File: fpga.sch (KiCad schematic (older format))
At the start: 4 parts

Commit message: FPGA change and new project file
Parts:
- removed U? (x4): XC6SLX9-2TQG144I, symbol FPGA_Xilinx_Spartan6:XC6SLX4-TQG144
- added U?: XC7S6-1FTGB196C, Xilinx-XC7S6-1FTGB196C-0-0-*, symbol sdr:XC7S6-1FTGB196C
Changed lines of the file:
@@
 $Descr A4 11693 8268
 encoding utf-8
-Sheet 1 1
+Sheet 1 12
 Title "Open HF SDR FPGA Sheet"
 Date "2021-01-16"
@@
 $EndDescr
 $Comp
-L FPGA_Xilinx_Spartan6:XC6SLX4-TQG144 U?
-U 1 1 6003554A
-P 3100 2500
-F 0 "U?" H 3100 725 50  0000 C CNN
-F 1 "XC6SLX9-2TQG144I" H 3100 634 50  0000 C CNN
-F 2 "" H 3100 2500 50  0001 C CNN
-F 3 "http://www.farnell.com/datasheets/1763510.pdf" H 3100 543 50  0000 C CNN
-F 4 "2831296 " H 3100 2500 50  0001 C CNN "Farnell"
-	1    3100 2500
+L sdr:XC7S6-1FTGB196C U?
+U 2 1 6006B8ED
+P 4150 1600
+F 0 "U?" H 6100 1865 50  0000 C CNN
+F 1 "XC7S6-1FTGB196C" H 6100 1774 50  0000 C CNN
+F 2 "Xilinx-XC7S6-1FTGB196C-0-0-*" H 4150 2000 50  0001 L CNN
+F 3 "https://www.xilinx.com/support/documentation/data_sheets/ds189-spartan-7-data-sheet.pdf" H 4150 2100 50  0001 L CNN
+F 4 "180Kbits" H 4150 2200 50  0001 L CNN "RAM size"
+F 5 "No" H 4150 2300 50  0001 L CNN "automotive"
+F 6 "IC" H 4150 2400 50  0001 L CNN "category"
+F 7 "Integrated Circuits (ICs)" H 4150 2500 50  0001 L CNN "device class L1"
+F 8 "Embedded Processors and Controllers" H 4150 2600 50  0001 L CNN "device class L2"
+F 9 "FPGAs - Field Programmable Gate Arrays" H 4150 2700 50  0001 L CNN "device class L3"
+F 10 "XC7S6-1FTGB196C" H 4150 2800 50  0001 L CNN "digikey description"
+F 11 "122-2240-ND" H 4150 2900 50  0001 L CNN "digikey part number"
+F 12 "https://www.xilinx.com/support/documentation/user_guides/ug475_7Series_Pkg_Pinout.pdf" H 4150 3000 50  0001 L CNN "footprint url"
+F 13 "200MHz" H 4150 3100 50  0001 L CNN "frequency"
+F 14 "1.55mm" H 4150 3200 50  0001 L CNN "height"
+F 15 "BGA196C100P14X14_1500X1500X146" H 4150 3300 50  0001 L CNN "ipc land pattern name"
+F 16 "Yes" H 4150 3400 50  0001 L CNN "lead free"
+F 17 "d5f555df3775b1ed" H 4150 3500 50  0001 L CNN "library id"
+F 18 "Xilinx" H 4150 3600 50  0001 L CNN "manufacturer"
+F 19 "+85°C" H 4150 3700 50  0001 L CNN "max junction temp"
+F 20 "3.465V" H 4150 3800 50  0001 L CNN "max supply voltage"
+F 21 "0.95V" H 4150 3900 50  0001 L CNN "min supply voltage"
+F 22 "100" H 4150 4000 50  0001 L CNN "number of I/Os"
+F 23 "938" H 4150 4100 50  0001 L CNN "number of logic blocks"
+F 24 "6000" H 4150 4200 50  0001 L CNN "number of logic elements cells"
+F 25 "FTGB196" H 4150 4300 50  0001 L CNN "package"
+F 26 "0.13ns" H 4150 4400 50  0001 L CNN "propagation delay"
+F 27 "Yes" H 4150 4500 50  0001 L CNN "rohs"
+F 28 "1" H 4150 4600 50  0001 L CNN "speed grade"
+F 29 "0.3mm" H 4150 4700 50  0001 L CNN "standoff height"
+F 30 "+85°C" H 4150 4800 50  0001 L CNN "temperature range high"
+F 31 "0°C" H 4150 4900 50  0001 L CNN "temperature range low"
+	2    4150 1600
 	1    0    0    -1
 $EndComp
-$Comp
-L FPGA_Xilinx_Spartan6:XC6SLX4-TQG144 U?
-U 2 1 6003A903
-P 8700 2550
-F 0 "U?" H 8700 775 50  0000 C CNN
-F 1 "XC6SLX9-2TQG144I" H 8700 684 50  0000 C CNN
-F 2 "" H 8700 2550 50  0001 C CNN
-F 3 "http://www.farnell.com/datasheets/1763510.pdf" H 8700 2550 50  0000 C CNN
-	2    8700 2550
-	1    0    0    -1
-$EndComp
-$Comp
-L FPGA_Xilinx_Spartan6:XC6SLX4-TQG144 U?
-U 3 1 60040928
-P 2700 5750
-F 0 "U?" H 2832 6517 50  0000 C CNN
-F 1 "XC6SLX9-2TQG144I" H 2832 6426 50  0000 C CNN
-F 2 "" H 2700 5750 50  0001 C CNN
-F 3 "http://www.farnell.com/datasheets/1763510.pdf" H 2700 5750 50  0000 C CNN
-	3    2700 5750
-	1    0    0    -1
-$EndComp
-$Comp
-L FPGA_Xilinx_Spartan6:XC6SLX4-TQG144 U?
-U 4 1 600436B6
-P 8700 5600
-F 0 "U?" H 8700 6467 50  0000 C CNN
-F 1 "XC6SLX9-2TQG144I" H 8700 6376 50  0000 C CNN
-F 2 "" H 8700 5600 50  0001 C CNN
-F 3 "http://www.farnell.com/datasheets/1763510.pdf" H 8700 5600 50  0000 C CNN
-	4    8700 5600
-	1    0    0    -1
-$EndComp

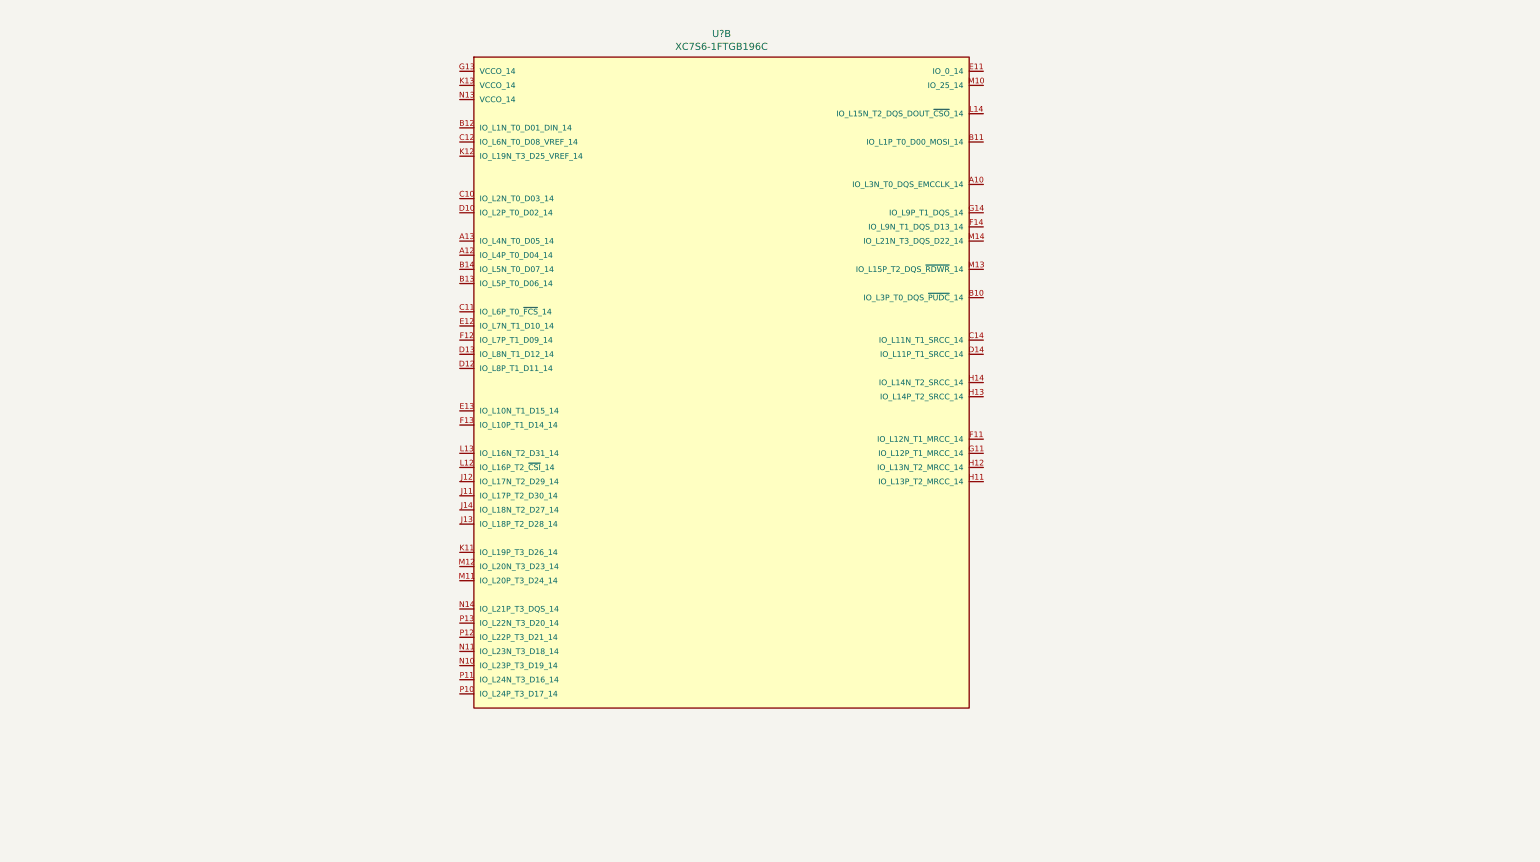
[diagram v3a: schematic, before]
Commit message: SDR-FPGA Interface v0
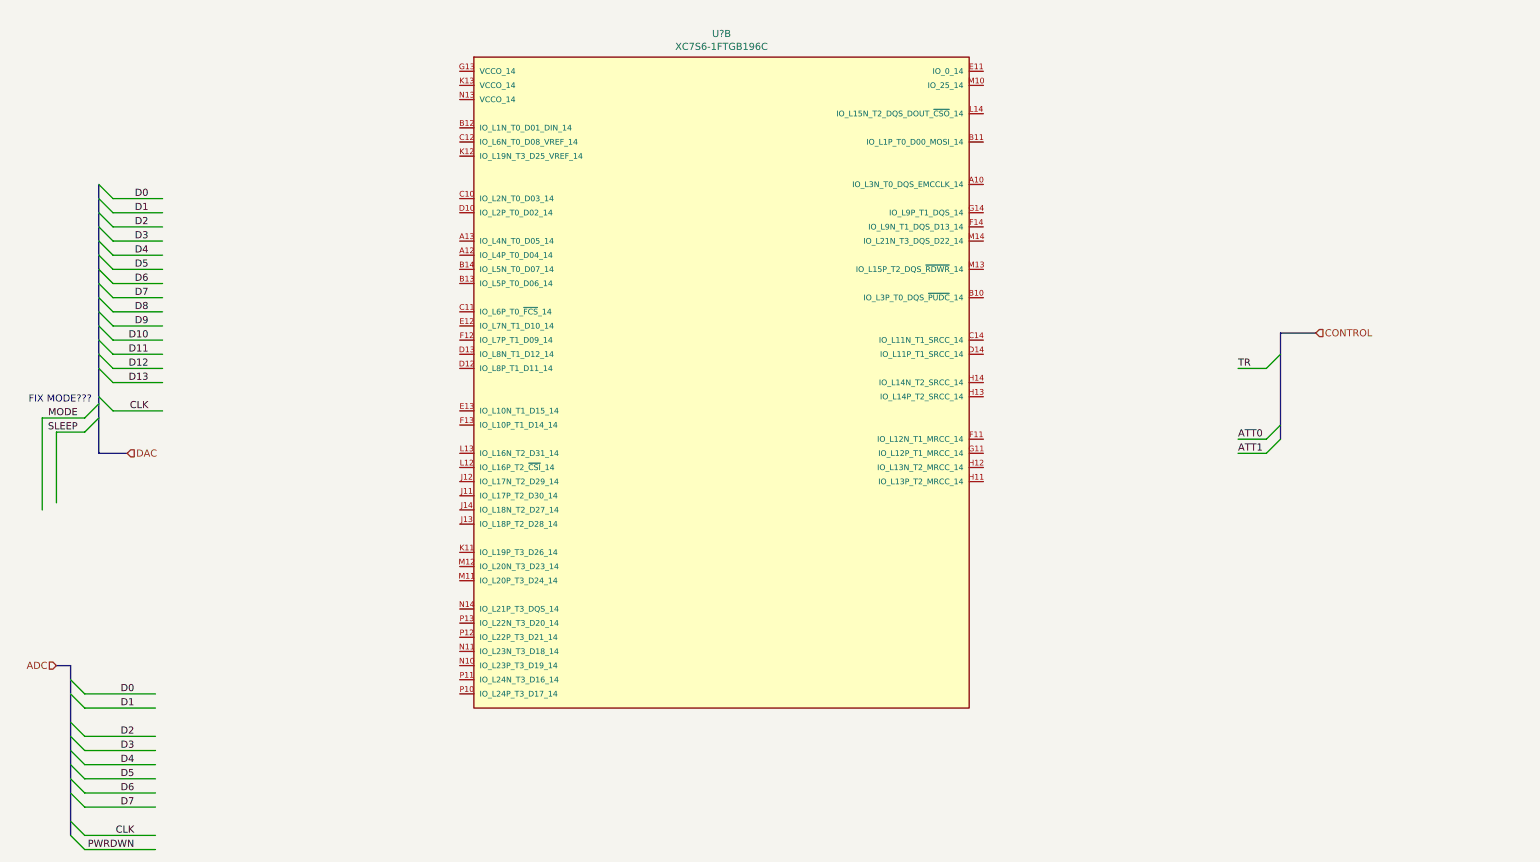
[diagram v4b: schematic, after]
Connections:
- net labels added: ADC, ATT0, ATT1, CLK, CONTROL, D0, D1, D10, D11, D12, D13, D2, D3, D4, D5, D6, D7, D8, D9, DAC, MODE, PWRDWN, SLEEP, TR
- wire segments 0 -> 32
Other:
- note added: "FIX MODE???"
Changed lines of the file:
@@
 	1    0    0    -1
 $EndComp
+Text HLabel 1400 5800 0    50   Input ~ 0
+ADC
+Entry Wire Line
+	1500 5900 1600 6000
+Entry Wire Line
+	1600 6100 1500 6000
+Entry Wire Line
+	1600 6300 1500 6200
+Entry Wire Line
+	1600 6400 1500 6300
+Entry Wire Line
+	1600 6500 1500 6400
+Entry Wire Line
+	1600 6600 1500 6500
+Entry Wire Line
+	1600 6700 1500 6600
+Entry Wire Line
+	1600 6800 1500 6700
+Entry Wire Line
+	1600 7000 1500 6900
+Entry Wire Line
+	1600 7100 1500 7000
+Wire Wire Line
+	2100 6000 1600 6000
+Wire Wire Line
+	2100 6100 1600 6100
+Wire Wire Line
+	1600 6300 2100 6300
+Wire Wire Line
+	2100 6400 1600 6400
+Wire Wire Line
+	2100 6500 1600 6500
+Wire Wire Line
+	2100 6600 1600 6600
+Wire Wire Line
+	2100 6700 1600 6700
+Wire Wire Line
+	2100 6800 1600 6800
+Wire Wire Line
+	2100 7000 1600 7000
+Wire Wire Line
+	2100 7100 1600 7100
+Text Label 1950 6000 2    50   ~ 0
+D0
+Text Label 1950 6100 2    50   ~ 0
+D1
+Text Label 1950 6300 2    50   ~ 0
+D2
+Text Label 1950 6400 2    50   ~ 0
+D3
+Text Label 1950 6500 2    50   ~ 0
+D4
+Text Label 1950 6600 2    50   ~ 0
+D5
+Text Label 1950 6700 2    50   ~ 0
+D6
+Text Label 1950 6800 2    50   ~ 0
+D7
+Text Label 1950 7000 2    50   ~ 0
+CLK
+Text Label 1950 7100 2    50   ~ 0
+PWRDWN
+Wire Bus Line
+	1500 5800 1400 5800
+Entry Wire Line
+	1800 2500 1700 2400
+Entry Wire Line
+	1800 2600 1700 2500
+Entry Wire Line
+	1800 2700 1700 2600
+Entry Wire Line
+	1800 2800 1700 2700
+Entry Wire Line
+	1800 2900 1700 2800
+Entry Wire Line
+	1800 3000 1700 2900
+Entry Wire Line
+	1800 3100 1700 3000
+Entry Wire Line
+	1800 3200 1700 3100
+Entry Wire Line
+	1800 3300 1700 3200
+Entry Wire Line
+	1800 3400 1700 3300
+Entry Wire Line
+	1800 3500 1700 3400
+Entry Wire Line
+	1800 3600 1700 3500
+Entry Wire Line
+	1800 3700 1700 3600
+Entry Wire Line
+	1800 3800 1700 3700
+Entry Wire Line
+	1800 4000 1700 3900
+Wire Wire Line
+	2150 2500 1800 2500
+Wire Wire Line
+	2150 2600 1800 2600
+Wire Wire Line
+	2150 2700 1800 2700
+Wire Wire Line
+	2150 2800 1800 2800
+Wire Wire Line
+	2150 2900 1800 2900
+Wire Wire Line
+	2150 3000 1800 3000
+Wire Wire Line
+	2150 3100 1800 3100
+Wire Wire Line
+	2150 3200 1800 3200
+Wire Wire Line
+	2150 3300 1800 3300
+Wire Wire Line
+	2150 3400 1800 3400
+Wire Wire Line
+	2150 3500 1800 3500
+Wire Wire Line
+	2150 3600 1800 3600
+Wire Wire Line
+	2150 3700 1800 3700
+Wire Wire Line
+	2150 3800 1800 3800
+Wire Wire Line
+	2150 4000 1800 4000
+Text Label 2050 2500 2    50   ~ 0
+D0
+Text Label 2050 2600 2    50   ~ 0
+D1
+Text Label 2050 2700 2    50   ~ 0
+D2
+Text Label 2050 2800 2    50   ~ 0
+D3
+Text Label 2050 2900 2    50   ~ 0
+D4
+Text Label 2050 3000 2    50   ~ 0
+D5
+Text Label 2050 3100 2    50   ~ 0
+D6
+Text Label 2050 3200 2    50   ~ 0
+D7
+Text Label 2050 3300 2    50   ~ 0
+D8
+Text Label 2050 3400 2    50   ~ 0
+D9
+Text Label 2050 3500 2    50   ~ 0
+D10
+Text Label 2050 3600 2    50   ~ 0
+D11
+Text Label 2050 3700 2    50   ~ 0
+D12
+Text Label 2050 3800 2    50   ~ 0
+D13
+Text Label 2050 4000 2    50   ~ 0
+CLK
+Wire Bus Line
+	1700 4300 1900 4300
+Text HLabel 1900 4300 2    50   Input ~ 0
+DAC
+Wire Wire Line
+	1400 4650 1400 4150
+Entry Wire Line
+	1700 4050 1600 4150
+Wire Wire Line
+	1600 4150 1400 4150
+Text Label 1550 4150 2    50   ~ 0
+SLEEP
+Wire Wire Line
+	1300 4700 1300 4050
+Wire Wire Line
+	1300 4050 1600 4050
+Entry Wire Line
+	1700 3950 1600 4050
+Text Label 1550 4050 2    50   ~ 0
+MODE
+Text Notes 1650 3950 2    50   ~ 0
+FIX MODE???
+Text Label 9750 4200 0    50   ~ 0
+ATT0
+Text Label 9750 4300 0    50   ~ 0
+ATT1
+Text Label 9750 3700 0    50   ~ 0
+TR
+Wire Bus Line
+	10050 3450 10300 3450
+Text HLabel 10300 3450 2    50   Input ~ 0
+CONTROL
+Entry Wire Line
+	9950 3700 10050 3600
+Entry Wire Line
+	9950 4300 10050 4200
+Entry Wire Line
+	9950 4200 10050 4100
+Wire Wire Line
+	9950 4200 9750 4200
+Wire Wire Line
+	9750 4300 9950 4300
+Wire Wire Line
+	9950 3700 9750 3700
+Wire Bus Line
+	10050 3450 10050 4200
+Wire Bus Line
+	1500 5800 1500 7000
+Wire Bus Line
+	1700 2400 1700 4300
 $EndSCHEMATC
